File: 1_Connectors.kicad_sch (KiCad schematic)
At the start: 3 parts, among them J1 PWR IN, J2 R-RJ45R08P-C000, J3 R-RJ45R08P-C000

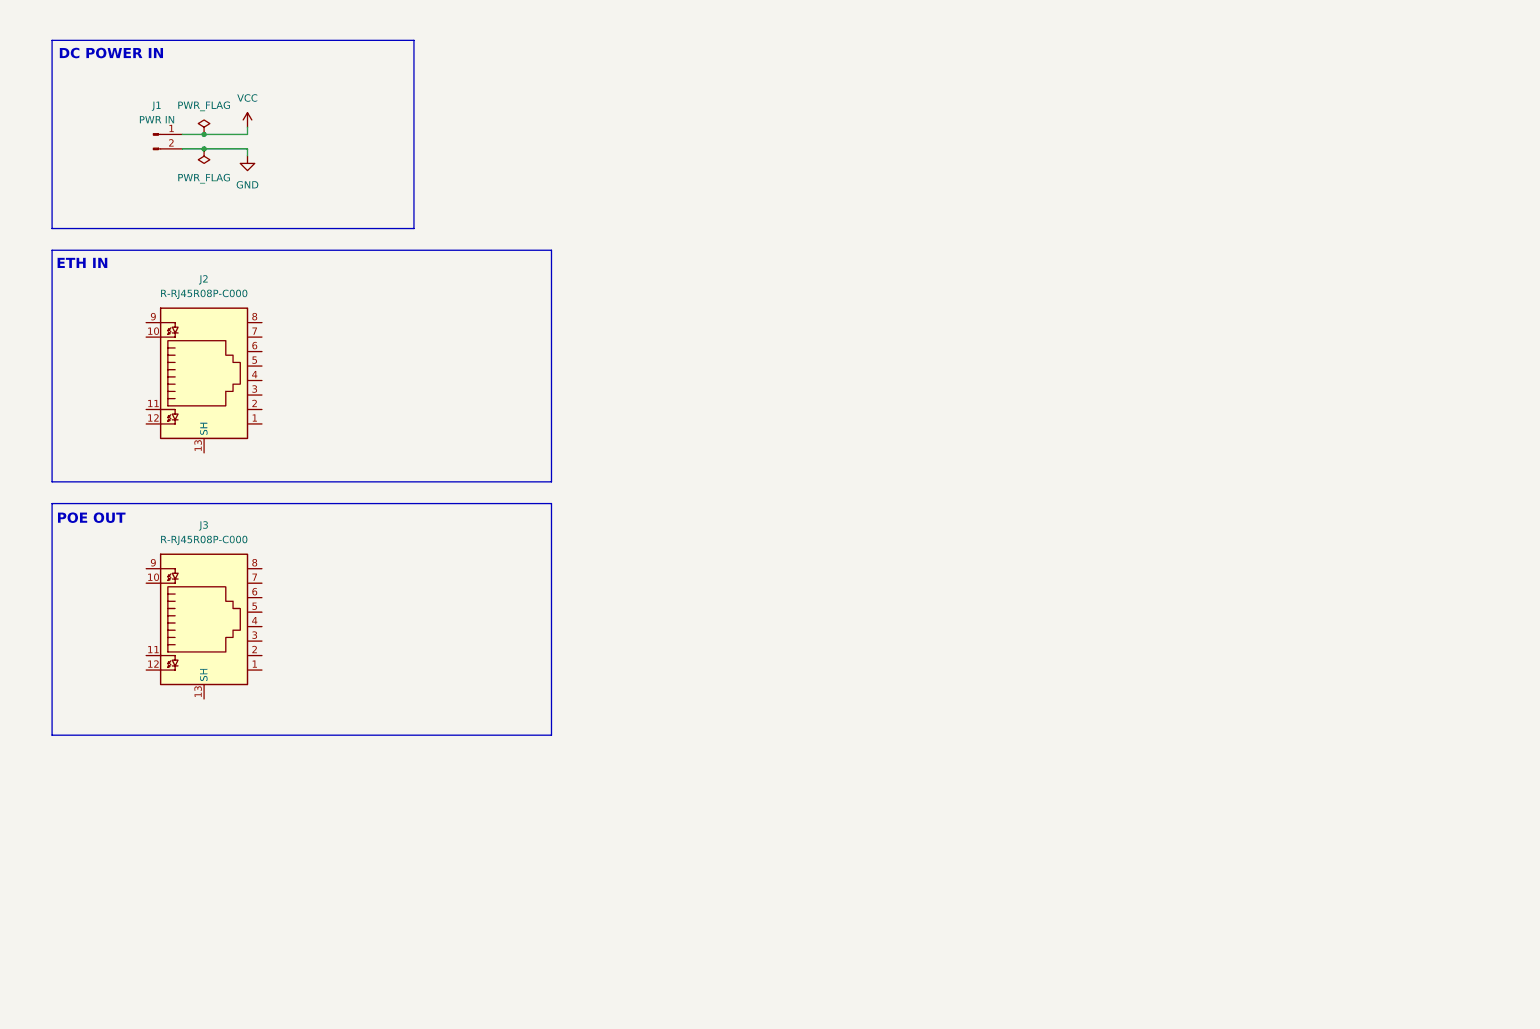
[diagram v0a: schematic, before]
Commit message: Add magnetics for poe
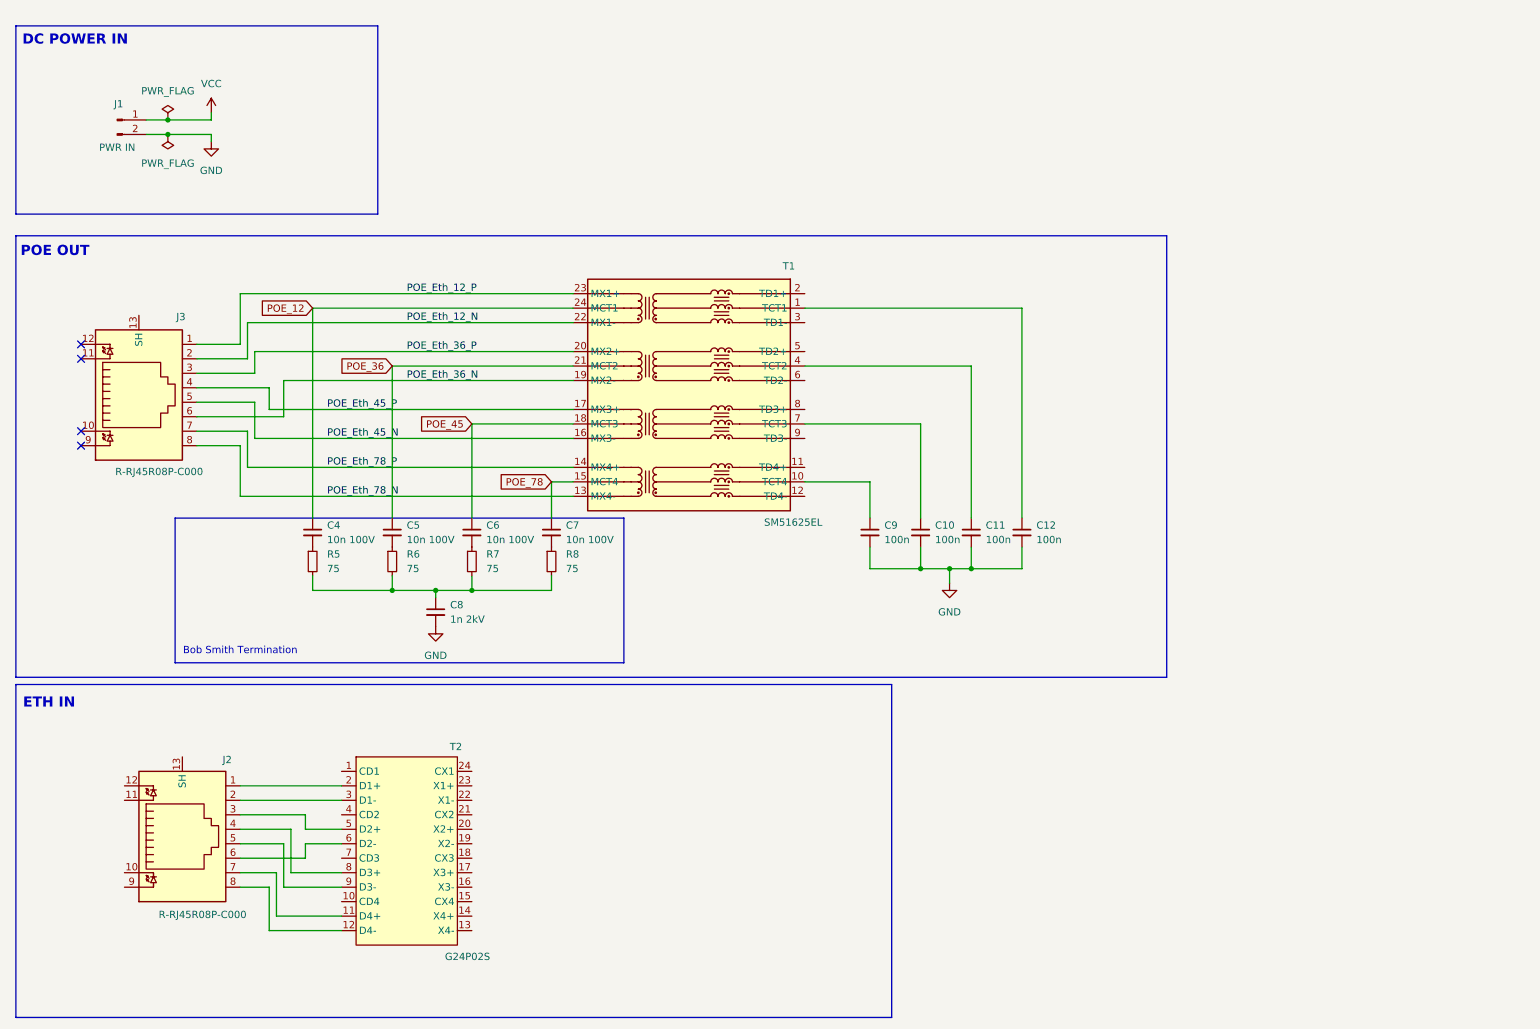
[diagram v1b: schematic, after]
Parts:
- added C10, C11, C12, C9: 100n, symbol Device:C_Small
- added C4, C5, C6, C7: 10n 100V, symbol Device:C_Small
- added C8: 1n 2kV, symbol Device:C_Small
- added R5, R6, R7, R8: 75, symbol Device:R_Small
- added T1: SM51625EL, CakeKiCadLib:SM51625EL, symbol CakeKiCadLib:SM51625EL
- added T2: G24P02S, CakeKiCadLib:G24P02S, symbol CakeKiCadLib:G24P02S
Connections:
- net GND: now also C10.2, C11.2, C12.2, C8.2, C9.2
- net POE_Eth_12_P: now reaches J3.1
- net POE_Eth_12_P: now also T1.23 (MX1+)
- net POE_Eth_12_N: now reaches J3.2
- net POE_Eth_12_N: now also T1.22 (MX1-)
- net POE_Eth_36_P: now reaches J3.3
- net POE_Eth_36_P: now also T1.20 (MX2+)
- net POE_Eth_45_P: now reaches J3.4
- net POE_Eth_45_P: now also T1.17 (MX3+)
- net POE_Eth_45_N: now reaches J3.5
- net POE_Eth_45_N: now also T1.16 (MX3-)
- net POE_Eth_36_N: now reaches J3.6
- net POE_Eth_36_N: now also T1.19 (MX2-)
- net POE_Eth_78_P: now reaches J3.7
- net POE_Eth_78_P: now also T1.14 (MX4+)
- net POE_Eth_78_N: now reaches J3.8
- net POE_Eth_78_N: now also T1.13 (MX4-)
- net at J2.1: now also T2.2 (D1+)
- net at J2.2: now also T2.3 (D1-)
- net at J2.3: now also T2.5 (D2+)
- net at J2.4: now also T2.8 (D3+)
- net at J2.5: now also T2.9 (D3-)
- net at J2.6: now also T2.6 (D2-)
- net at J2.7: now also T2.11 (D4+)
- net at J2.8: now also T2.12 (D4-)
- new net: C11.1, T1.4 (TCT2)
- new net: C4.2, R5.1
- new net: C10.1, T1.7 (TCT3)
- new net: C12.1, T1.1 (TCT1)
- new net: C9.1, T1.10 (TCT4)
- new net: C5.2, R6.1
- new net: C8.1, R5.2, R6.2, R7.2, R8.2
- new net: C7.2, R8.1
- new net: C6.2, R7.1
- new net POE_12: C4.1, T1.24 (MCT1)
- new net POE_36: C5.1, T1.21 (MCT2)
- new net POE_45: C6.1, T1.18 (MCT3)
- new net POE_78: C7.1, T1.15 (MCT4)
- no-connect marks 0 -> 4
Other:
- note added: "Bob Smith Termination"
- moved on the sheet: J1, J2, J3

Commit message: Add boost converter
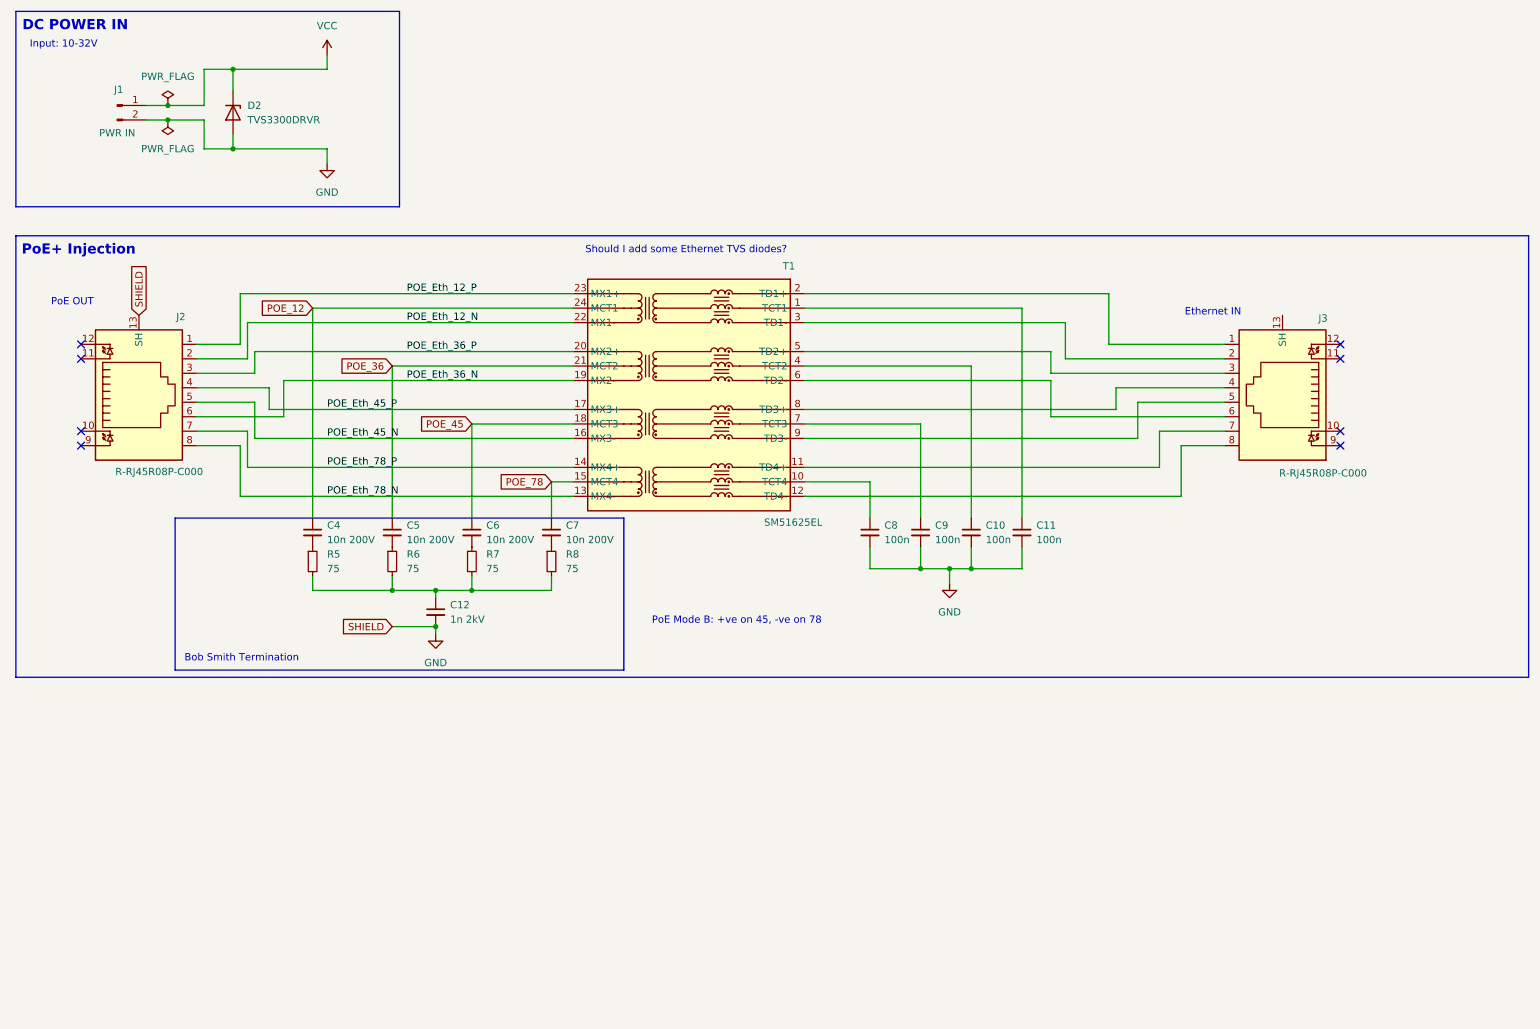
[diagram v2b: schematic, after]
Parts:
- removed T2: G24P02S, CakeKiCadLib:G24P02S, symbol CakeKiCadLib:G24P02S
- added D2: TVS3300DRVR, symbol Device:D_Zener
- C4, C5, C6, C7: value 10n 100V -> 10n 200V
- renumbered C11 to C10, C12 to C11, C8 to C12, C9 to C8, C10 to C9, J3 to J2, J2 to J3
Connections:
- net GND: now also J2.13 (SH), D2.2 (A)
- net VCC: now also D2.1 (K)
- net at T1.11 (TD4+): now also J3.7
- net at T1.12 (TD4-): now also J3.8
- net at T1.2 (TD1+): now also J3.1
- net at T1.3 (TD1-): now also J3.2
- net at T1.5 (TD2+): now also J3.3
- net at T1.6 (TD2-): now also J3.6
- net at T1.8 (TD3+): now also J3.4
- net at T1.9 (TD3-): now also J3.5
- no-connect marks 4 -> 8
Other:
- note added: "Ethernet IN"
- note added: "Input: 10-32V"
- note added: "PoE Mode B: +ve on 45, -ve on 78"
- note added: "PoE OUT"
- note added: "PoE+ Injection"
- note added: "Should I add some Ethernet TVS diodes?"
- note removed: "ETH IN"
- note removed: "POE OUT"
- moved on the sheet: J1, J3

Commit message: finish layout
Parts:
- removed D2: TVS3300DRVR, symbol Device:D_Zener
- added C13: 1n 2kV, Capacitor_SMD:C_1206_3216Metric, symbol Device:C_Small
- added D2: TVS3300DRVx, CakeKiCadLib:DRV0006A, symbol CakeKiCadLib:TVS3300DRVx
- added H1, H2, H3, H4: MountingHole, MountingHole:MountingHole_3.2mm_M3, symbol Mechanical:MountingHole
- added R10, R11, R12, R9: 75, Resistor_SMD:R_0805_2012Metric, symbol Device:R_Small
- C10, C11, C8, C9: value 100n -> 10n 200V; footprint (none) -> Capacitor_SMD:C_0805_2012Metric; LCSC (none) -> C106844
- C12: footprint (none) -> Capacitor_SMD:C_1206_3216Metric; LCSC (none) -> C9196
- C4, C5, C6, C7: footprint (none) -> Capacitor_SMD:C_0805_2012Metric; LCSC (none) -> C106844
- J1: footprint (none) -> Connector_Phoenix_SPT:PhoenixContact_SPT_2.5_2-H-5.0_1x02_P5.0mm_Horizontal; LCSC (none) -> C5443538
- R5, R6, R7, R8: footprint (none) -> Resistor_SMD:R_0805_2012Metric; LCSC (none) -> C20638
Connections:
- net GND: now also J3.13 (SH), C13.2, D2.1 (A), D2.2 (A), D2.3 (A), D2.7 (A); no longer C10.2, C11.2, C8.2, C9.2
- net POE_Eth_12_N: now also J2.1; no longer J2.2
- net POE_Eth_12_P: now also J2.2; no longer J2.1
- net VCC: now also D2.4 (K), D2.5 (K), D2.6 (K)
- net EthIN_78_N: now reaches J3.7
- net EthIN_78_N: now also T1.12 (TD4-); no longer T1.11 (TD4+)
- net EthIN_78_P: now reaches J3.8
- net EthIN_78_P: now also T1.11 (TD4+); no longer T1.12 (TD4-)
- net EthIN_12_P: now reaches J3.1, T1.2 (TD1+)
- net EthIN_12_N: now reaches J3.2, T1.3 (TD1-)
- net EthIN_36_P: now reaches J3.3, T1.5 (TD2+)
- net EthIN_36_N: now reaches J3.6, T1.6 (TD2-)
- net EthIN_45_N: now reaches J3.4
- net EthIN_45_N: now also T1.9 (TD3-); no longer T1.8 (TD3+)
- net EthIN_45_P: now reaches J3.5
- net EthIN_45_P: now also T1.8 (TD3+); no longer T1.9 (TD3-)
- new net: C11.2, R12.1
- new net: C13.1, R10.2, R11.2, R12.2, R9.2
- new net: C8.2, R9.1
- new net: C9.2, R10.1
- new net: C10.2, R11.1
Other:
- note added: "Input: 12-32V"
- note removed: "Input: 10-32V"
- title: (none) -> DC Midspan 802.3at PoE Injector
- moved on the sheet: J3
